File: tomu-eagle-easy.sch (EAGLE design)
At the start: 18 parts, among them U1 EFM32HG309F64G

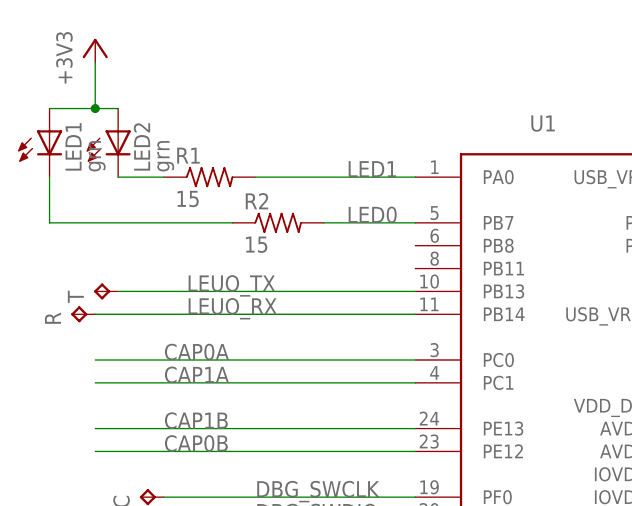
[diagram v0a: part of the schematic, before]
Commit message: LED resistors should be 75 not 15 (or maybe 52 as in the tomu bom)
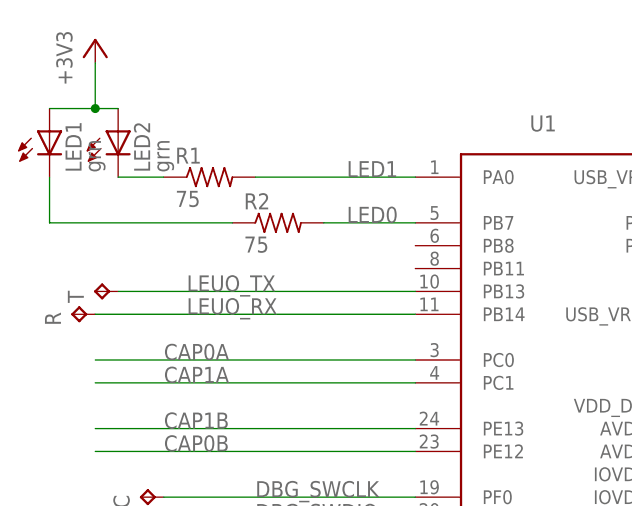
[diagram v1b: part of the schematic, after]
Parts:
- R1, R2: value 15 -> 75
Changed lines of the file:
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@@
 <?xml version="1.0" encoding="utf-8"?>
 <!DOCTYPE eagle SYSTEM "eagle.dtd">
-<eagle version="8.6.3">
+<eagle version="8.7.1">
 <drawing>
 <settings>
@@
 <part name="GND3" library="supply1" library_urn="urn:adsk.eagle:library:371" deviceset="GND" device=""/>
 <part name="+3V2" library="supply1" library_urn="urn:adsk.eagle:library:371" deviceset="+3V3" device=""/>
-<part name="R1" library="adafruit" library_urn="urn:adsk.eagle:library:420" deviceset="R-US_" device="R0402" value="15"/>
-<part name="R2" library="adafruit" library_urn="urn:adsk.eagle:library:420" deviceset="R-US_" device="R0402" value="15"/>
+<part name="R1" library="adafruit" library_urn="urn:adsk.eagle:library:420" deviceset="R-US_" device="R0402" value="75"/>
+<part name="R2" library="adafruit" library_urn="urn:adsk.eagle:library:420" deviceset="R-US_" device="R0402" value="75"/>
 <part name="LED1" library="adafruit" library_urn="urn:adsk.eagle:library:420" deviceset="LED" device="CHIP-LED0603" value="grn"/>
 <part name="LED2" library="adafruit" library_urn="urn:adsk.eagle:library:420" deviceset="LED" device="CHIP-LED0603" value="grn"/>
